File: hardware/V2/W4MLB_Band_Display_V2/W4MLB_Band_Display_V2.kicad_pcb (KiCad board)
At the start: 2 copper layers, 95.8 x 64.5 mm, 26 parts, among them J1 SSW-115-01-G-S, J2 SSW-115-01-G-S, J3 SSQ-108-01-T-D-LL, J4 SAMTEC-TST-108-01-X-D, J5 PJRAN1X1U01X, J6 PJRAN1X1U01X, J7 FHP-04-01-X-S, J8 EJ503B, J9 Conn_01x09, Q1 MMBT2222A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

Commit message: Adjustment to parts locations
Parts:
- moved J7 0.41 mm to (209.0, 93.5)
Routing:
- net GND: track 7.58 -> 6.57 mm
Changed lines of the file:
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@@
 		(tags "diode handsolder")
 		(property "Reference" "D1"
-			(at -3.125 0.05 0)
+			(at -0.025 1.85 0)
 			(layer "F.SilkS")
 			(effects
@@
 		(tags "LED handsolder")
 		(property "Reference" "D3"
-			(at -4.525 0 0)
+			(at 2.925 0 0)
 			(layer "F.SilkS")
 			(effects
@@
 		)
 		(embedded_fonts no)
+		(model "C:/Users/sapy4/Documents/PCARS_Band_Display/hardware/V2/Libraries/3DModels/1812L300SLPR.step"
+			(offset
+				(xyz 0 0 1)
+			)
+			(scale
+				(xyz 1 1 1)
+			)
+			(rotate
+				(xyz 90 -0 -0)
+			)
+		)
 	)
 	(footprint "Diode_SMD:D_0805_2012Metric_Pad1.15x1.40mm_HandSolder"
@@
 		(tags "diode handsolder")
 		(property "Reference" "D2"
-			(at -3.125 0 0)
+			(at -0.025 -2 0)
 			(layer "F.SilkS")
 			(effects
@@
 		(locked yes)
 		(layer "B.Cu")
-		(at 209.03 93.0987 -90)
+		(at 209.03 93.5087 -90)
 		(property "Reference" "J7"
-			(at -10.4987 -0.1 90)
+			(at -10.0887 -0.1 90)
 			(layer "B.SilkS")
 			(effects
@@
 		)
 		(property "Value" "FHP-04-01-X-S"
-			(at -0.1987 4.13 90)
+			(at 0.2113 4.13 90)
 			(layer "B.Fab")
 			(effects
@@
 	)
 	(gr_rect
-		(start 206.22 93.49)
-		(end 211.68 100.44)
+		(start 206.04 93.71)
+		(end 212.04 100.88)
 		(stroke
 			(width 0.125)
@@
 	)
 	(gr_rect
-		(start 206.22 85.21)
-		(end 211.71 92.74)
+		(start 206 85.8)
+		(end 212.01 92.81)
 		(stroke
 			(width 0.125)
@@
 	)
 	(gr_line
-		(start 205.79 85.12)
-		(end 204.14 85.12)
+		(start 205.79 85.53)
+		(end 204.14 85.53)
 		(stroke
 			(width 0.125)
@@
 	)
 	(gr_line
-		(start 204.14 85.12)
-		(end 204.1 92.6)
+		(start 204.14 85.53)
+		(end 204.1 93.01)
 		(stroke
 			(width 0.125)
@@
 	)
 	(gr_line
-		(start 204.1 92.6)
-		(end 205.74 92.6)
+		(start 204.1 93.01)
+		(end 205.74 93.01)
 		(stroke
 			(width 0.125)
@@
 	)
 	(gr_text "GND"
-		(at 207.5 102 0)
+		(at 207.5 102.9 0)
 		(layer "F.SilkS")
 		(effects
@@
 	)
 	(gr_text "Plug directly\ninto HUB75	\nLED Matrix"
-		(at 203 88.5 90)
+		(at 203 88.91 90)
 		(layer "B.SilkS")
 		(effects
@@
 	)
 	(gr_text "+5V"
-		(at 205.8 87.2 90)
+		(at 205.8 87.61 90)
 		(layer "B.SilkS")
 		(effects
@@
 	)
 	(gr_text "GND"
-		(at 205.8 95.6 90)
+		(at 205.8 96.01 90)
 		(layer "B.SilkS")
 		(effects
@@
 	)
 	(segment
+		(start 205.54 101.2)
+		(end 204.625 101.2)
+		(width 0.4)
+		(layer "F.Cu")
+		(net 1)
+	)
+	(segment
 		(start 126.575 82)
 		(end 127.98 82)
@@
 	)
 	(segment
-		(start 204.5 102.6)
-		(end 204.5 101.25)
-		(width 0.4)
-		(layer "F.Cu")
-		(net 1)
-	)
-	(segment
-		(start 209.875 74.5)
+		(start 209.3 74.5)
 		(end 207.75 74.5)
 		(width 0.4)
@@
 	)
 	(via
-		(at 209.875 74.5)
+		(at 209.3 74.5)
 		(size 0.7)
 		(drill 0.4)
@@
 	)
 	(via
-		(at 204.5 102.6)
+		(at 205.54 101.2)
 		(size 0.7)
 		(drill 0.4)

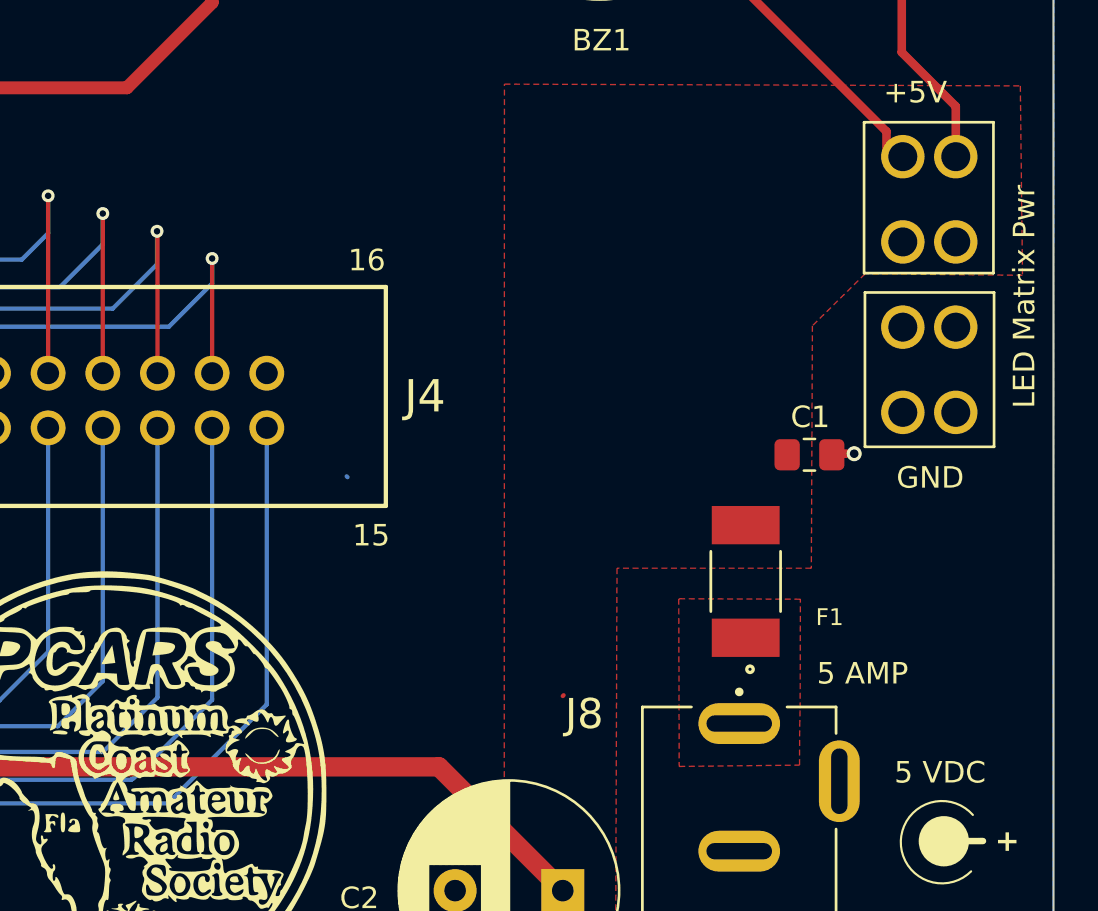
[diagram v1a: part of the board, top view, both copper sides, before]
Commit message: Updates to V1 & V2 boards
Updated location of +5V LED Matric power connector on V2 board after careful measurements.
Made final changes to V1 board before sending off to fabrication.
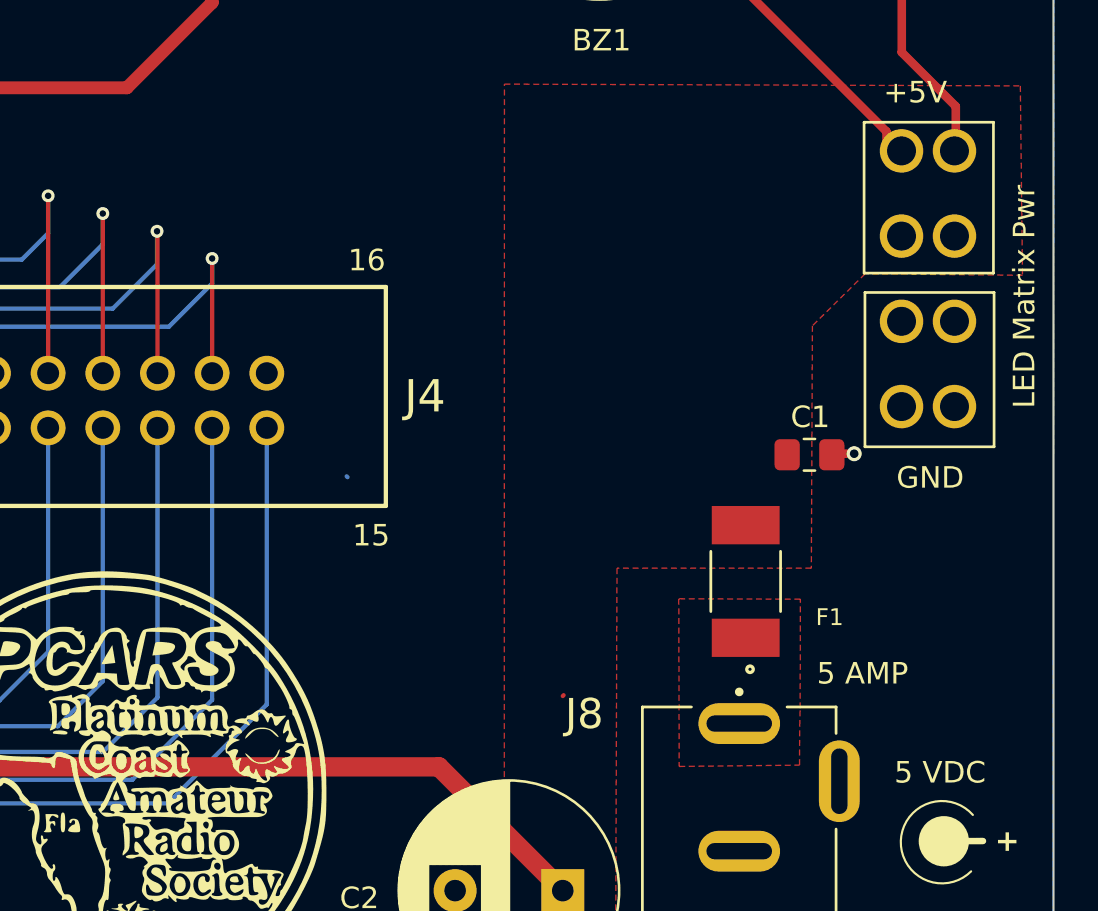
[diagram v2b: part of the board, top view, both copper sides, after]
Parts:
- moved J7 0.28 mm to (209.0, 93.2)
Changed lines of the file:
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@@
 		(locked yes)
 		(layer "B.Cu")
-		(at 209.03 93.5087 -90)
+		(at 208.97 93.2387 -90)
 		(property "Reference" "J7"
 			(at -10.0887 -0.1 90)
@@
 	)
 	(segment
-		(start 172.05 116.3)
+		(start 172 116.35)
 		(end 175.71 112.64)
 		(width 0.2)
@@
 	)
 	(segment
-		(start 171.953857 116.35)
-		(end 172.05 116.253857)
+		(start 125.2 99.2825)
+		(end 125.2 107.7)
 		(width 0.2)
 		(layer "B.Cu")
@@
 	)
 	(segment
-		(start 125.2 99.2825)
-		(end 125.2 107.7)
+		(start 171.953857 116.35)
+		(end 172 116.35)
 		(width 0.2)
 		(layer "B.Cu")
